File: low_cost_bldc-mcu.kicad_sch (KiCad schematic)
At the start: 1 part, among them U1 CH32V003FxUx

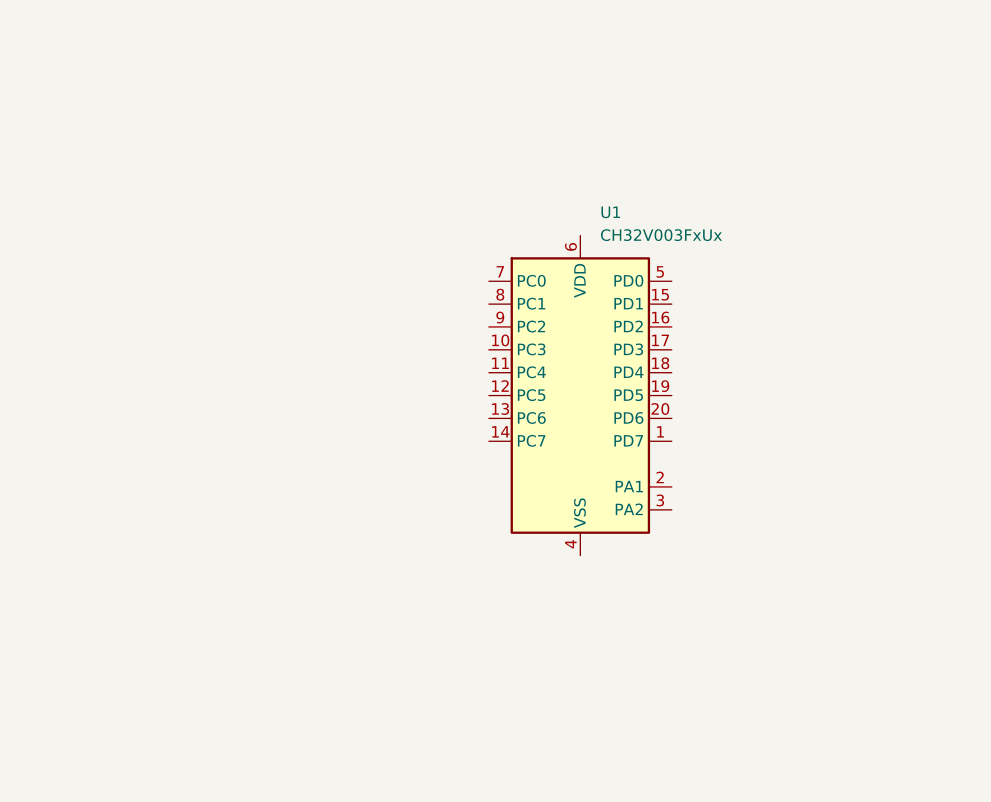
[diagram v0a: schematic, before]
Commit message: Top-only inverter layout
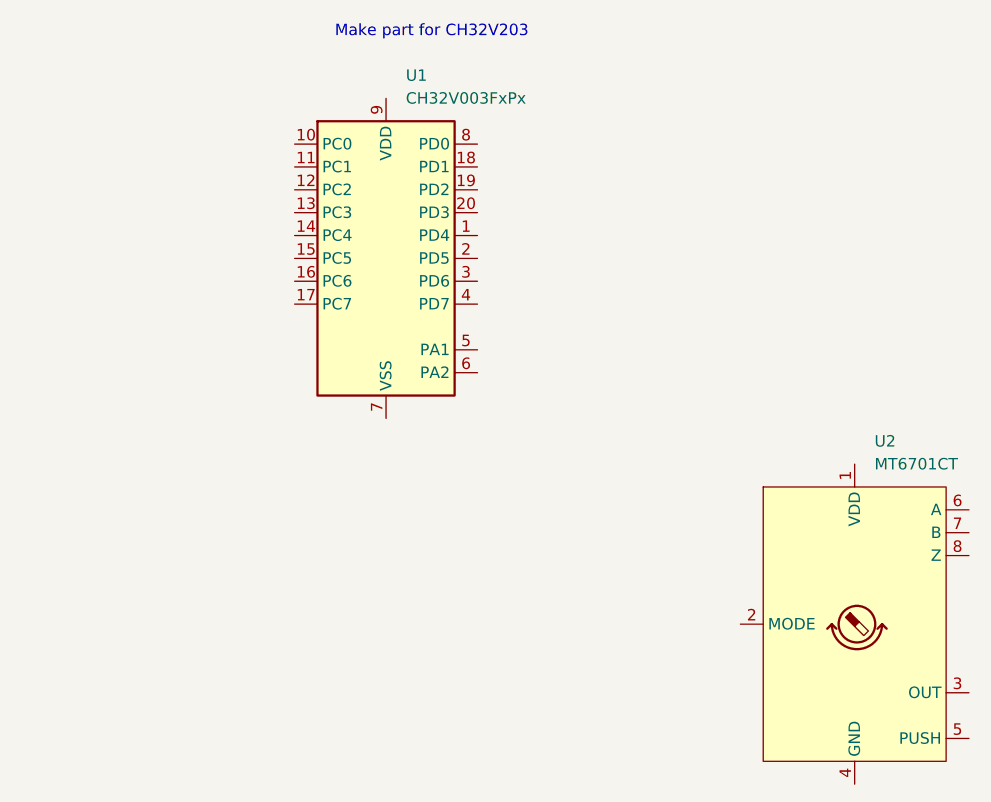
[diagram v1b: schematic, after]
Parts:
- removed U1: CH32V003FxUx, Package_DFN_QFN:QFN-20-1EP_3x3mm_P0.4mm_EP1.65x1.65mm, symbol MCU_WCH_CH32V0:CH32V003FxUx
- added U1: CH32V003FxPx, Package_SO:TSSOP-20_4.4x6.5mm_P0.65mm, symbol MCU_WCH_CH32V0:CH32V003FxPx
- added U2: MT6701CT, Package_SO:SO-8_3.9x4.9mm_P1.27mm, symbol Sensor_Magnetic:MT6701CT
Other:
- note added: "Make part for CH32V203"
- title: (none) -> FreeWheel

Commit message: Readme, rough connector placement, inverter refinement, increase MCU pin count to have a chance of succeeding.
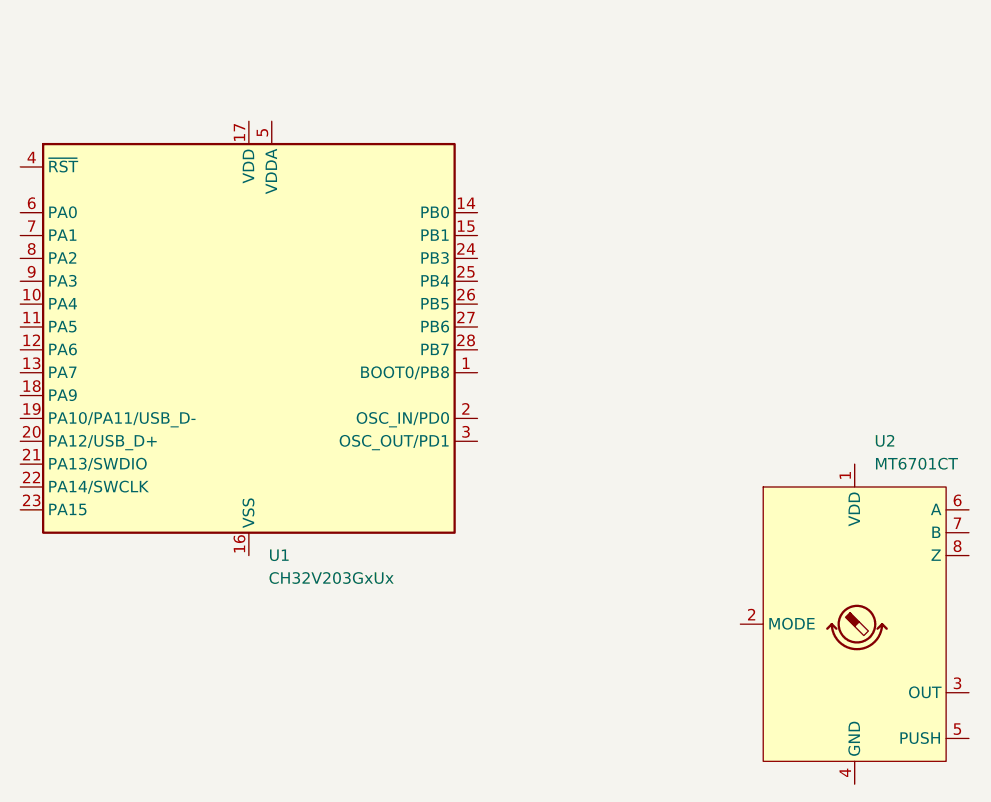
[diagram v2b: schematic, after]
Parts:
- removed U1: CH32V003FxPx, Package_SO:TSSOP-20_4.4x6.5mm_P0.65mm, symbol MCU_WCH_CH32V0:CH32V003FxPx
- added U1: CH32V203GxUx, Package_DFN_QFN:QFN-28-1EP_4x4mm_P0.4mm_EP2.7x2.7mm, symbol MCU_WCH_CH32V2:CH32V203GxUx
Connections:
- new net: U1.16 (VSS), U1.29 (VSS)
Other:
- note removed: "Make part for CH32V203"
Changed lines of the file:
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@@
-		)
-	)
-	(text "Make part for CH32V203"
-		(exclude_from_sim no)
-		(at 143.51 51.054 0)
-		(effects
-			(font
-				(size 1.27 1.27)
-			)
 		)
 	)
 	(symbol
-		(lib_id "MCU_WCH_CH32V0:CH32V003FxPx")
-		(at 138.43 76.2 0)
+		(lib_id "MCU_WCH_CH32V2:CH32V203GxUx")
+		(at 123.19 86.36 0)
 		(unit 1)
 		(exclude_from_sim no)
@@
 		(fields_autoplaced yes)
 		(property "Reference" "U1"
-			(at 140.6241 55.88 0)
+			(at 125.3841 109.22 0)
 			(effects
 				(font
@@
 			)
 		)
-		(property "Value" "CH32V003FxPx"
-			(at 140.6241 58.42 0)
+		(property "Value" "CH32V203GxUx"
+			(at 125.3841 111.76 0)
 			(effects
 				(font
@@
 			)
 		)
-		(property "Footprint" "Package_SO:TSSOP-20_4.4x6.5mm_P0.65mm"
-			(at 137.16 76.2 0)
+		(property "Footprint" "Package_DFN_QFN:QFN-28-1EP_4x4mm_P0.4mm_EP2.7x2.7mm"
+			(at 90.17 107.95 0)
 			(effects
 				(font
@@
 			)
 		)
-		(property "Datasheet" "https://www.wch-ic.com/products/CH32V003.html"
-			(at 137.16 76.2 0)
+		(property "Datasheet" "https://www.wch-ic.com/downloads/CH32V203DS0_PDF.html"
+			(at 123.19 49.276 0)
 			(effects
 				(font
@@
 			)
 		)
-		(property "Description" "CH32V003 series are industrial-grade general-purpose microcontrollers designed based on 32-bit RISC-V instruction set and architecture. It adopts QingKe V2A core, RV32EC instruction set, and supports 2 levels of interrupt nesting. The series are mounted with rich peripheral interfaces and function modules. Its internal organizational structure meets the low-cost and low-power embedded application scenarios."
-			(at 138.43 76.2 0)
+		(property "Description" "NanjingQinheng WCH RISC-V MCU, 32-64KB flash, 10-20KB RAM, 144 MHz, 2.4-3.6V, 24 GPIO, ADC, OpAmp, CAN, USB, QFN-28"
+			(at 122.682 46.99 0)
 			(effects
 				(font
@@
 			)
 		)
+		(pin "26"
+		)
+		(pin "24"
+		)
+		(pin "2"
+		)
+		(pin "20"
+		)
+		(pin "25"
+		)
+		(pin "8"
+		)
+		(pin "6"
+		)
+		(pin "19"
+		)
+		(pin "16"
+		)
+		(pin "9"
+		)
+		(pin "22"
+		)
+		(pin "27"
+		)
+		(pin "11"
+		)
+		(pin "10"
+		)
+		(pin "29"
+		)
 		(pin "3"
+		)
+		(pin "12"
+		)
+		(pin "21"
+		)
+		(pin "17"
 		)
 		(pin "18"
 		)
-		(pin "14"
-		)
-		(pin "8"
-		)
-		(pin "19"
-		)
-		(pin "17"
-		)
-		(pin "10"
-		)
-		(pin "20"
+		(pin "4"
 		)
 		(pin "7"
 		)
-		(pin "5"
-		)
-		(pin "6"
+		(pin "1"
 		)
 		(pin "13"
 		)
-		(pin "4"
-		)
-		(pin "16"
-		)
-		(pin "12"
-		)
-		(pin "11"
-		)
-		(pin "9"
+		(pin "28"
 		)
 		(pin "15"
 		)
-		(pin "2"
+		(pin "14"
 		)
-		(pin "1"
+		(pin "23"
+		)
+		(pin "5"
 		)
 		(instances
